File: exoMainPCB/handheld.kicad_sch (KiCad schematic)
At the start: 14 parts, among them J4 HDMI_A, J5 USB_A

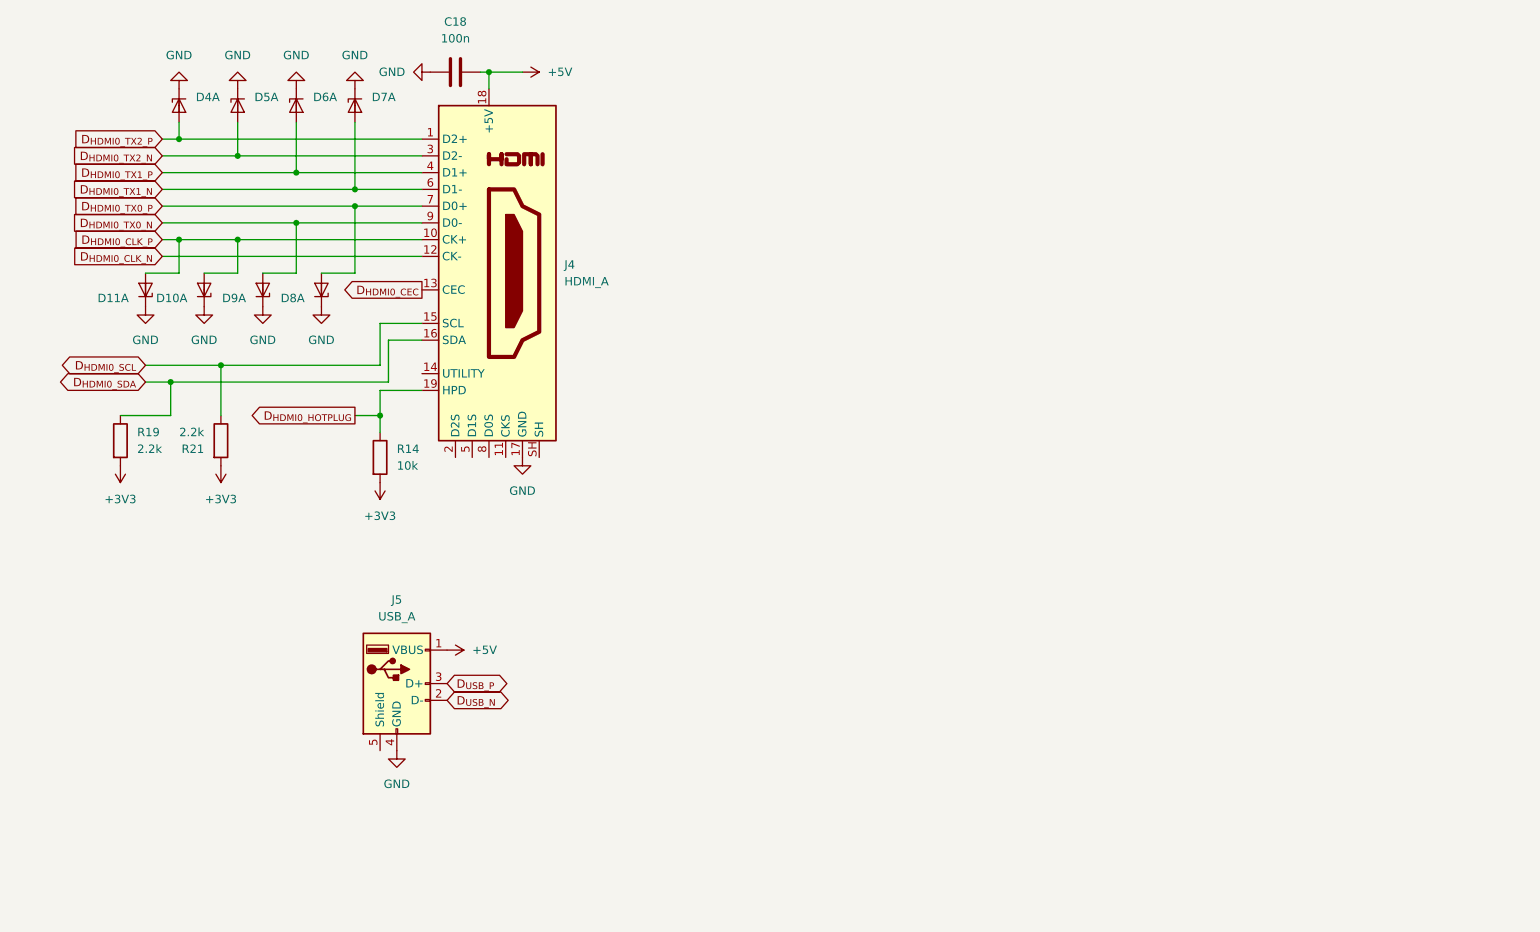
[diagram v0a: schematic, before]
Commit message: changed all resistors to US, updated IO, finished Handheld
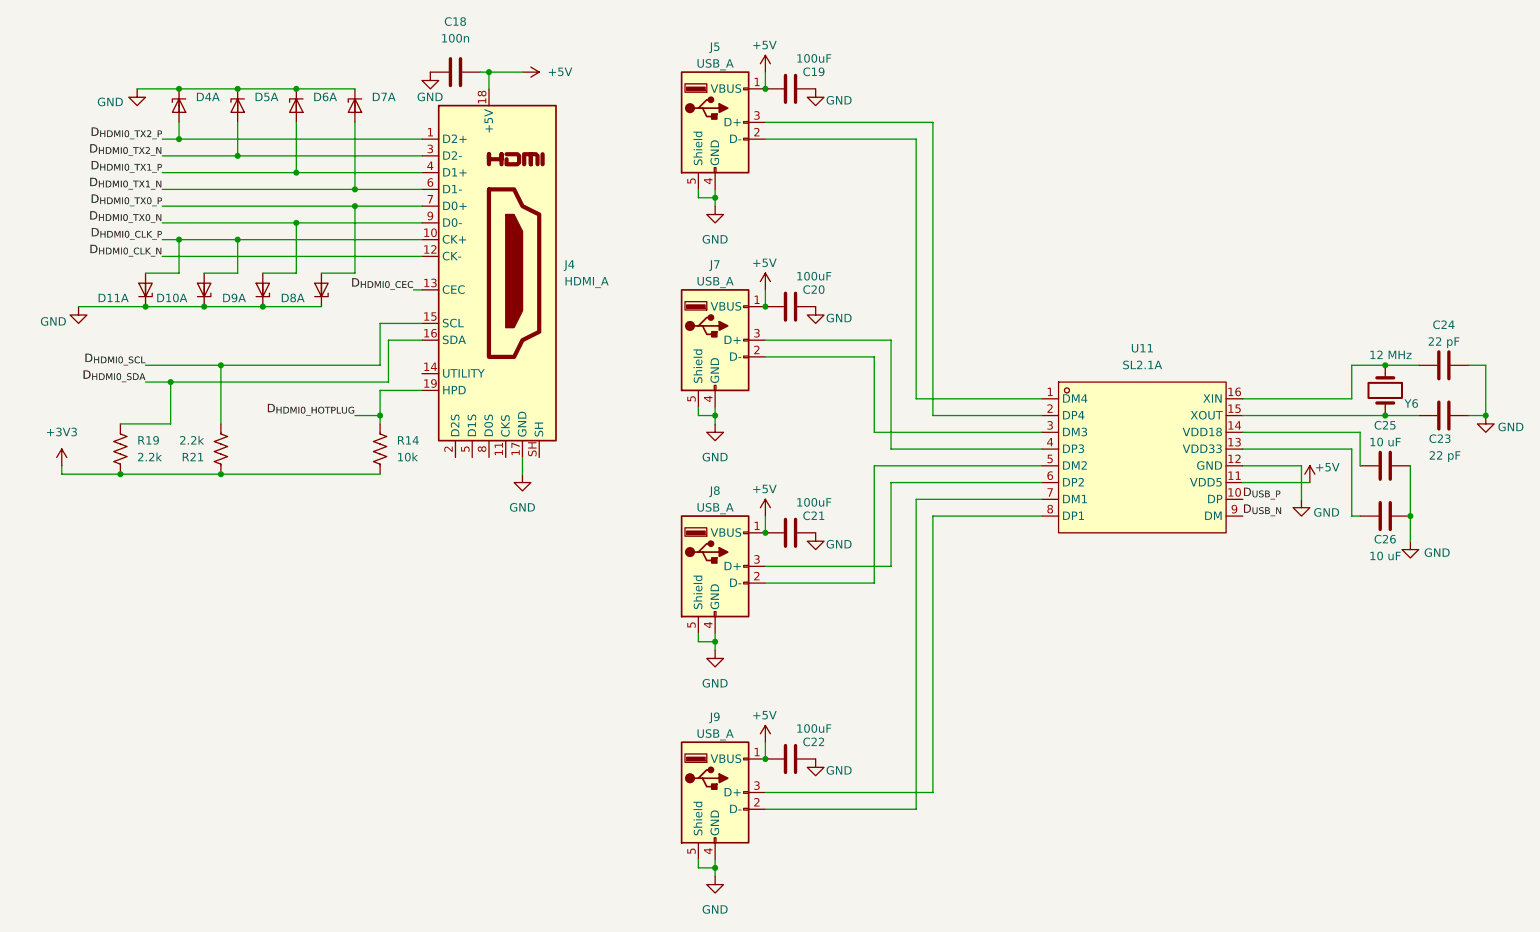
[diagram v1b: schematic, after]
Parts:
- added C19, C20, C21, C22: 100uF, symbol Device:C
- added C23, C24: 22 pF, symbol Device:C
- added C25, C26: 10 uF, symbol Device:C
- added J7, J8, J9: USB_A, symbol Connector:USB_A
- added U11: SL2.1A, my_lib:SOP-16_L10.0-W3.9-P1.27-LS6.0-BL, symbol SL2.1A:SL2.1A
- added Y6: 12 MHz, symbol Device:Crystal
- R14, R19, R21: symbol Device:R -> Device:R_US
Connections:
- net +5V: now also C19.1, C20.1, C21.1, C22.1, J7.1 (VBUS), J8.1 (VBUS), J9.1 (VBUS), U11.11 (VDD5)
- net D_{USB_N}: now also U11.9 (DM); no longer J5.2 (D-)
- net D_{USB_P}: now also U11.10 (DP); no longer J5.3 (D+)
- net GND: now also J5.5 (Shield), C19.2, C20.2, C21.2, C22.2, C23.1, C24.1, C25.1, C26.1, J7.4 (GND), J7.5 (Shield), J8.4 (GND), J8.5 (Shield), J9.4 (GND), J9.5 (Shield), U11.12 (GND)
- new net: J9.2 (D-), U11.7 (DM1)
- new net: J9.3 (D+), U11.8 (DP1)
- new net: C25.2, U11.14 (VDD18)
- new net: C23.2, U11.15 (XOUT), Y6.2
- new net: C24.2, U11.16 (XIN), Y6.1
- new net: J5.2 (D-), U11.1 (DM4)
- new net: J5.3 (D+), U11.2 (DP4)
- new net: C26.2, U11.13 (VDD33)
- new net: J8.2 (D-), U11.5 (DM2)
- new net: J8.3 (D+), U11.6 (DP2)
- new net: J7.2 (D-), U11.3 (DM3)
- new net: J7.3 (D+), U11.4 (DP3)
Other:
- moved on the sheet: J5
